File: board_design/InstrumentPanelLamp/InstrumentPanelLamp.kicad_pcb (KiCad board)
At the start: 2 copper layers, 164.5 x 33.5 mm, 53 parts, among them J1 male_spade, J10 male_spade, J11 male_spade, J12 male_spade, J13 male_spade, J14 Conn_01x02_Pin, J18 Conn_01x02_Pin, J19 Conn_01x02_Pin, J2 male_spade, J20 Conn_01x02_Pin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

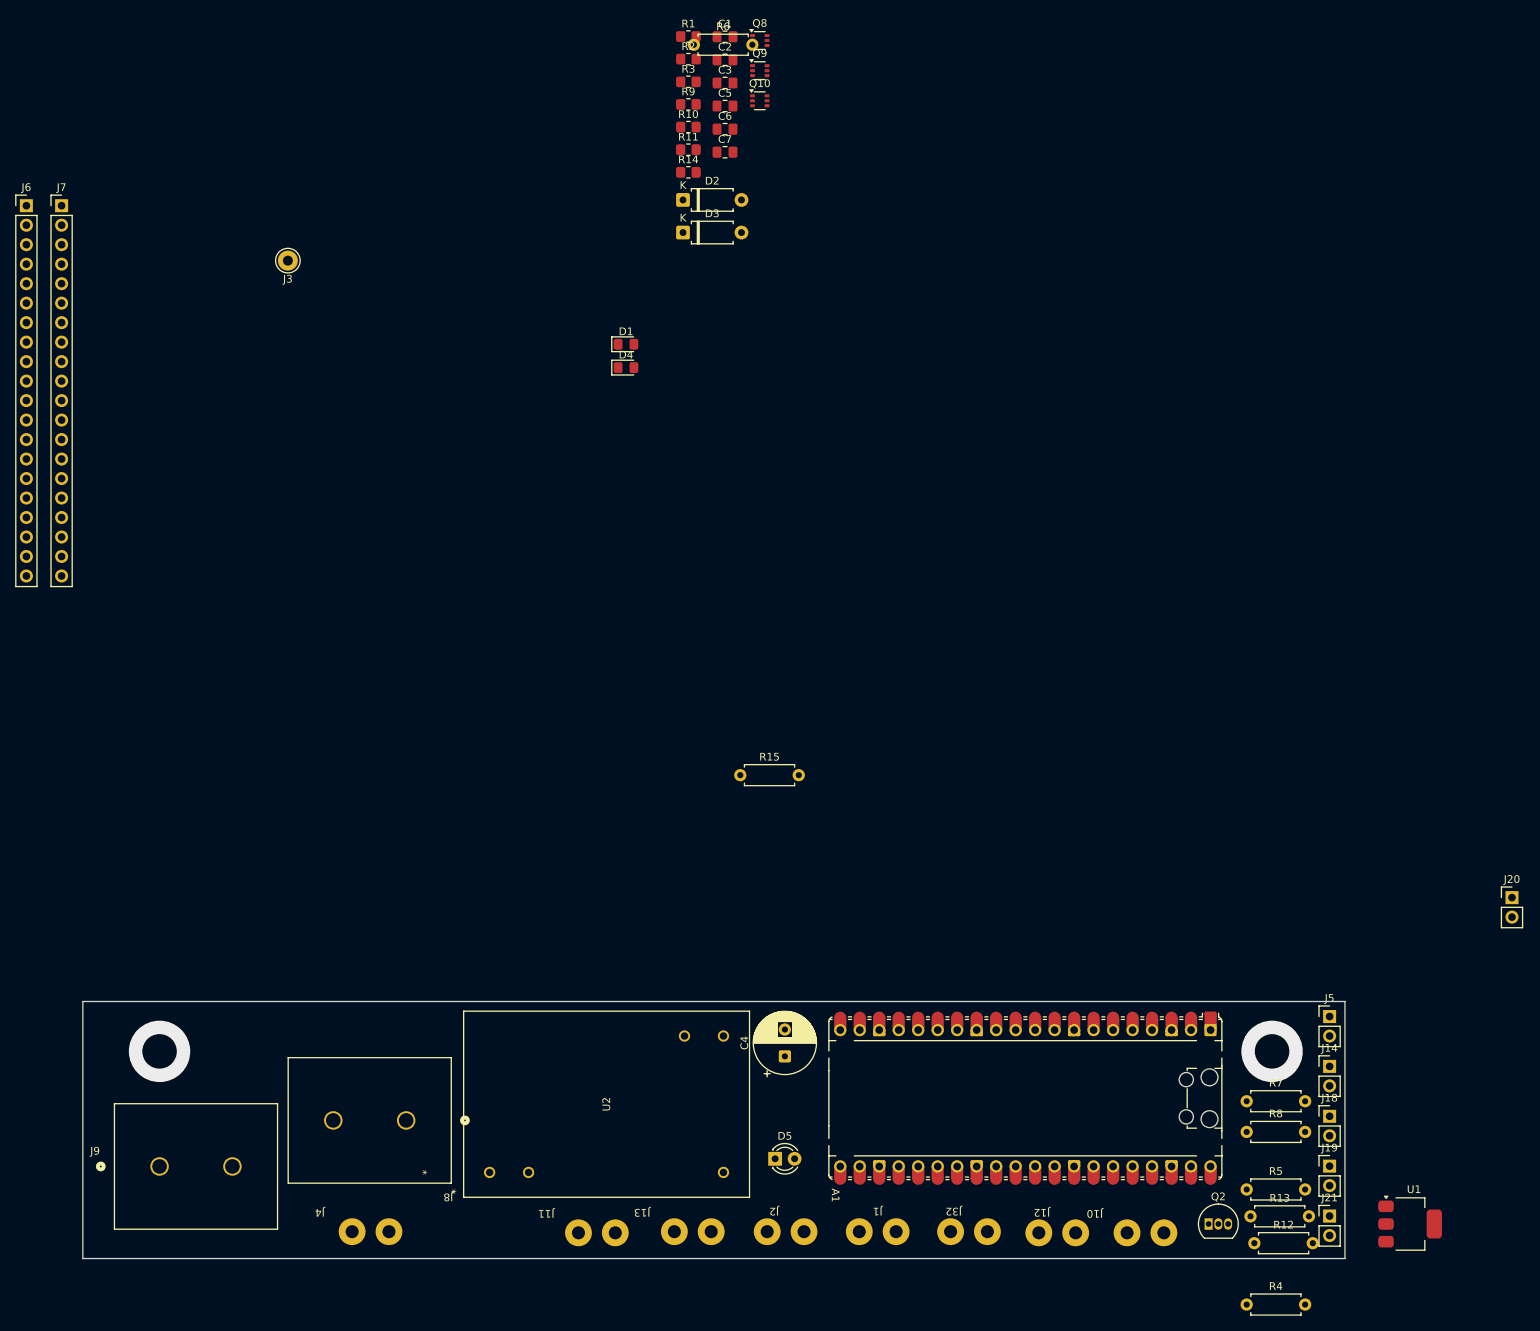
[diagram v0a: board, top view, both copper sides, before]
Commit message: Complete initial version of Arduino code and initial PCB placement
The arduino sketch is now as functional as the old version was.
The kicab pcb file has the initial placement of components done as
well using the updated Arduino pro mini as the MCU.
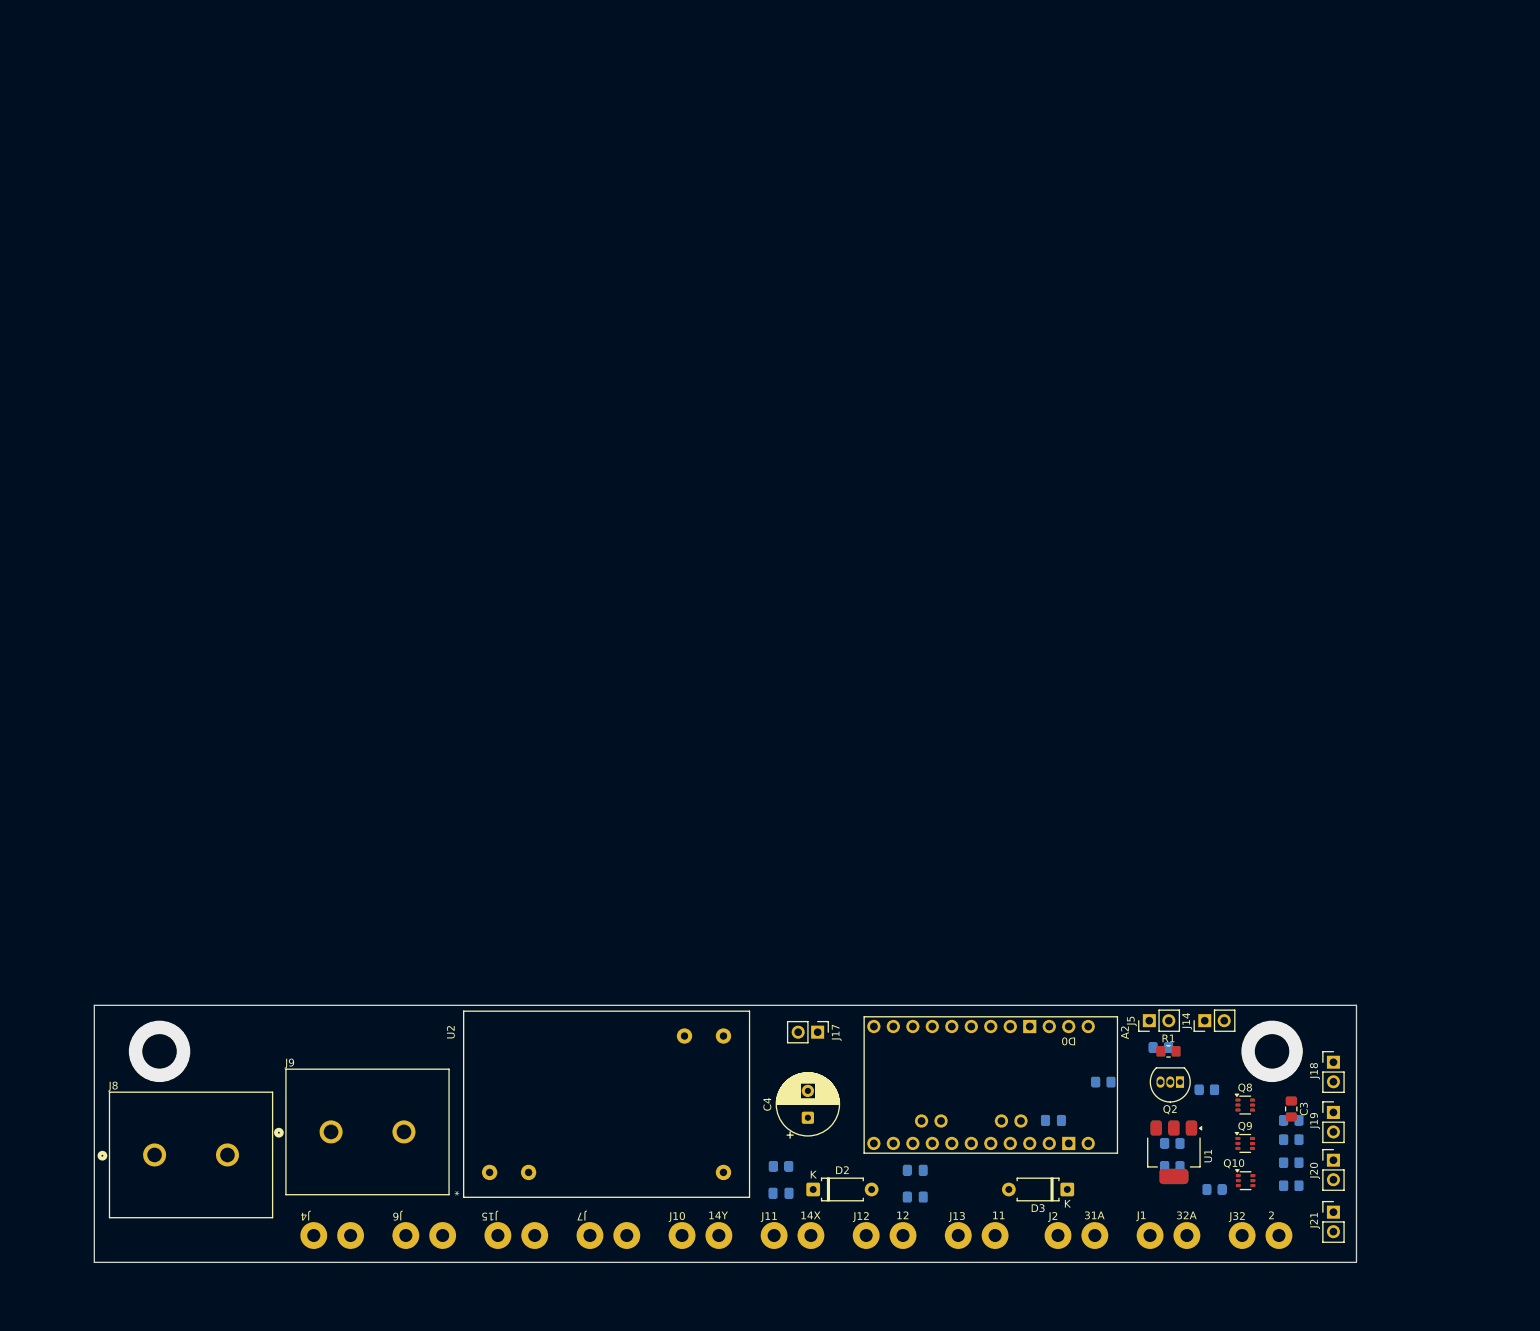
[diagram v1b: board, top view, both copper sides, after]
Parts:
- removed A1: RaspberryPi_Pico, Module:RaspberryPi_Pico_Common_Unspecified
- removed C7: 0.1uF, Capacitor_SMD:C_0805_2012Metric_Pad1.18x1.45mm_HandSolder
- removed D1: D_Zener, Diode_SMD:D_0805_2012Metric_Pad1.15x1.40mm_HandSolder
- removed D4: LED, Diode_SMD:D_0805_2012Metric_Pad1.15x1.40mm_HandSolder
- removed D5: PWR_LED, LED_THT:LED_D3.0mm
- removed J3: Mounting_Hole, Connector_Pin:Pin_D1.3mm_L11.0mm
- removed R11: 1k, Resistor_SMD:R_0805_2012Metric_Pad1.20x1.40mm_HandSolder
- removed R14: 220, Resistor_SMD:R_0805_2012Metric_Pad1.20x1.40mm_HandSolder
- removed R15: 200, Resistor_THT:R_Axial_DIN0207_L6.3mm_D2.5mm_P7.62mm_Horizontal
- added A2: Arduino_Pro_Mini_Socket_NoSPH, PCM_arduino-library:Arduino_Pro_Mini_Socket_NoSPH, F.Cu at (191.3, 100.9)
- added J15: NC, InstrumentPanelLamp:Keystone_4914_90deg_spade_male, F.Cu at (129.5, 120.5)
- added J17: pwr_tp, Connector_PinHeader_2.54mm:PinHeader_1x02_P2.54mm_Vertical, F.Cu at (168.8, 94.0)
- C1, C2, C5, C6, R10, R2, R3, R9: moved to B.Cu
- C3: value 0.1uF -> 10uF
- C4: value 10uF -> 47uF
- J1: value male_spade -> knob_gnd
- J10: value male_spade -> red_gnd
- J11: value male_spade -> red_in
- J12: value male_spade -> blk_gnd
- J13: value male_spade -> blk_in
- J14: value Conn_01x02_Pin -> aux2_conn
- J18: value Conn_01x02_Pin -> white_led_conn
- J19: value Conn_01x02_Pin -> red_led_conn
- J2: value male_spade -> knob_pos
- J20: value Conn_01x02_Pin -> green_led_conn
- J21: value Conn_01x02_Pin -> blue_led_conn
- J32: value male_spade -> knob_in
- J4: value male_spade -> lamp_out
- J5: value Conn_01x02_Pin -> aux1_conn
- J6, J7: value Conn_01x20_Socket -> NC; footprint Connector_PinHeader_2.54mm:PinHeader_1x20_P2.54mm_Vertical -> InstrumentPanelLamp:Keystone_4914_90deg_spade_male
- J8: value 2 pin screw terminal -> vac_in screw terminal
- J9: value 2 pin screw terminal -> lamp_screw_terminal
- R12, R13, R4, R5, R6, R7, R8: footprint Resistor_THT:R_Axial_DIN0207_L6.3mm_D2.5mm_P7.62mm_Horizontal -> Resistor_SMD:R_0805_2012Metric_Pad1.20x1.40mm_HandSolder; moved to B.Cu
- moved R6 165.2 mm to (230.5, 111.0), turned to 180 degrees
- moved Q10 154.3 mm to (224.6, 113.3)
- moved Q9 153.5 mm to (224.5, 108.5)
- moved C3 152.7 mm to (230.5, 104.0), turned to -90 degrees
- moved Q8 152.5 mm to (224.5, 103.5)
- moved R3 152.1 mm to (215.0, 108.5), turned to 180 degrees
- moved J7 152.0 mm to (141.5, 120.5), turned to 180 degrees
- moved C1 147.6 mm to (199.5, 105.5)
- moved C2 146.8 mm to (181.5, 112.0), turned to 180 degrees
- moved R1 146.3 mm to (214.5, 96.5)
- moved R9 145.1 mm to (219.5, 101.5), turned to 180 degrees
- moved J6 143.9 mm to (117.5, 120.5), turned to 180 degrees
- moved R2 143.9 mm to (206.0, 100.5), turned to 180 degrees
- moved C5 141.9 mm to (164.0, 115.0), turned to 180 degrees
- moved C6 141.4 mm to (181.5, 115.5), turned to 180 degrees
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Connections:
- C1 pad 1: +3.3V -> +5V
- C3 pad 2: ADC_VREF -> 5V
- C4 pad 1: blue_led_pos -> +5V
- J14 pad 2: aux_2_pos -> 5V
- J18 pad 2: blue_led_pos -> 5V
- J19 pad 2: blue_led_pos -> 5V
- J20 pad 2: blue_led_pos -> 5V
- J21 pad 2: blue_led_pos -> 5V
- J5 pad 2: aux_1_pos -> 5V
- J6 pad 1: uart_pi_tx -> unconnected-(J6-Pin_1-Pad1)
- J7 pad 1: debug_led_out -> unconnected-(J7-Pin_1-Pad1)
- U2 pad 16: blue_led_pos -> +5V
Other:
- board text added: "11"
- board text added: "12"
- board text added: "14X"
- board text added: "14Y"
- board text added: "2"
- board text added: "31A"
- board text added: "32A"

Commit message: board: Update board/sch design files with 3d model changes
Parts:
- removed Q2: BC327, Package_TO_SOT_THT:TO-92_Inline
- added Q1: DMG2302U, Package_TO_SOT_SMD:SOT-23, F.Cu at (213.5, 101.6)
- C3: moved to B.Cu
- C5, C6, R10, R12, R13, R5, R6, R7, R8: moved to F.Cu
- D2: footprint Diode_THT:D_A-405_P7.62mm_Horizontal -> Diode_SMD:D_SMA_Handsoldering; moved to B.Cu
- D3: footprint Diode_THT:D_A-405_P7.62mm_Horizontal -> Diode_SMD:D_SMA_Handsoldering
- moved D2 34.3 mm to (202.5, 114.5), turned to 180 degrees
- moved R9 33.1 mm to (189.5, 115.5), turned to 0 degrees
- moved R13 16.5 mm to (221.0, 98.0), turned to -90 degrees
- moved C3 13.4 mm to (232.8, 117.2)
- moved C2 6.02 mm to (187.5, 111.5)
- moved C5 5.47 mm to (169.0, 112.8), turned to 90 degrees
- moved R12 4.92 mm to (218.0, 98.0), turned to -90 degrees
- moved R3 3.72 mm to (217.5, 111.2), turned to 90 degrees
- moved R2 3.01 mm to (206.2, 97.5)
- moved R8 2.50 mm to (230.5, 103.0)
- moved R4 2.14 mm to (213.0, 112.2), turned to 0 degrees
- moved C6 2.00 mm to (183.5, 115.5), turned to 0 degrees
- moved R5 1.75 mm to (230.5, 106.2)
- moved D3 1.69 mm to (203.0, 114.5)
- moved R1 1.41 mm to (213.5, 97.5), turned to 180 degrees
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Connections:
- net Net-(Q2-B) renamed /logic/pch_gate
- A2 pad D12: unconnected-(A2-D12_MISO-PadD12) -> aux1
- A2 pad D13: unconnected-(A2-D13_SCK-PadD13) -> aux2
- C3 pad 2: 5V -> +5V
- J14 pad 2: 5V -> +5V
- J18 pad 2: 5V -> +5V
- J19 pad 2: 5V -> +5V
- J20 pad 2: 5V -> +5V
- J21 pad 2: 5V -> +5V
- J5 pad 2: 5V -> +5V
- Q10 pad 2: GPIO21 -> aux1
- Q10 pad 5: GPIO22 -> aux2
- R1 pad 1: 5V -> +5V
- R10 pad 1: 5V -> +5V
- R9 pad 1: 5V -> +5V
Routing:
- net +5V: track 0.00 -> 192.7 mm, vias 0 -> 3
- net blue_led_out: track 0.00 -> 57.9 mm, vias 0 -> 4
- net aux1: track 0.00 -> 53.7 mm, vias 0 -> 2
- net knob_meas_in: track 0.00 -> 52.9 mm, vias 0 -> 2
- net green_led_out: track 0.00 -> 52.4 mm, vias 0 -> 2
- net aux2: track 0.00 -> 51.2 mm
- net white_led_out: track 0.00 -> 50.6 mm, vias 0 -> 4
- net VAC_IN_N: track 0.00 -> 47.5 mm
- net VAC_IN_L_FUSED: track 0.00 -> 46.2 mm
- net red_led_out: track 0.00 -> 44.8 mm, vias 0 -> 2
- net GND: track 0.00 -> 38.8 mm, vias 0 -> 6
- net knob_power_control: track 0.00 -> 29.3 mm
- net knob_supply_pos: track 0.00 -> 26.2 mm
- net black_button_in: track 0.00 -> 25.9 mm
- net red_button_in: track 0.00 -> 25.5 mm
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- added copper zone on B.Cu, net GND
- added copper zone on F.Cu, net Net-(R4-Pad2)
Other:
- board text added: "+"
- board text added: "B"
- board text added: "G"
- board text added: "R"
- board text added: "Scott Stack 2025"
- board text added: "W"
- board text added: "angry electrons here >:("
- board text added: "blk_gnd"
- board text added: "blk_in"
- board text added: "knob+"
- board text added: "knob-"
- board text added: "knob_in"
- board text added: "lamp out"
- board text added: "oh hi!"
- board text added: "red_gnd"
- board text added: "red_in"
